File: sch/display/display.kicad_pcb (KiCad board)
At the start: 2 copper layers, 76.2 x 45.7 mm, 17 parts, among them IC1 MAX7219, P1 INPUT, P2 CONN_1, P3 CONN_1, P4 CONN_1, P5 CONN_1, P6 OUTPUT

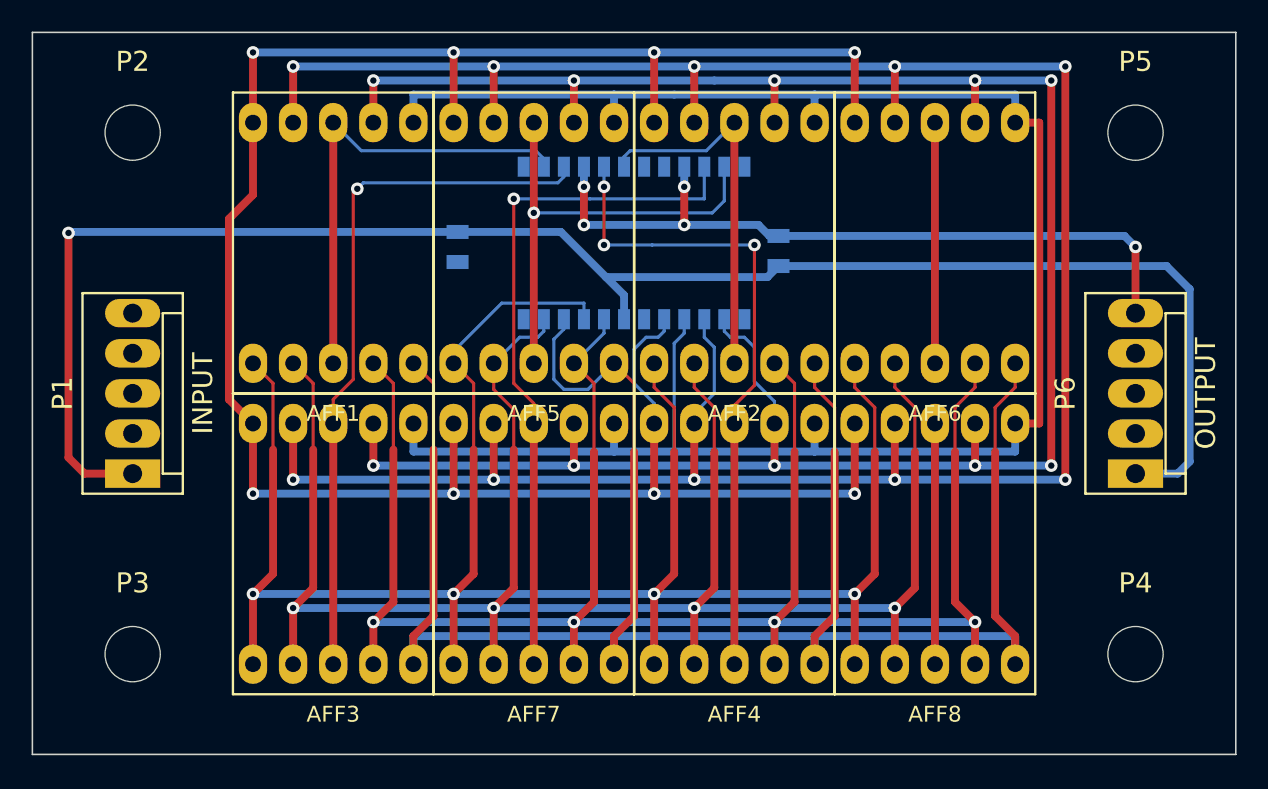
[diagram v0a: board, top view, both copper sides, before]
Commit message: Finished layout of the display.  Not really happy with it though.
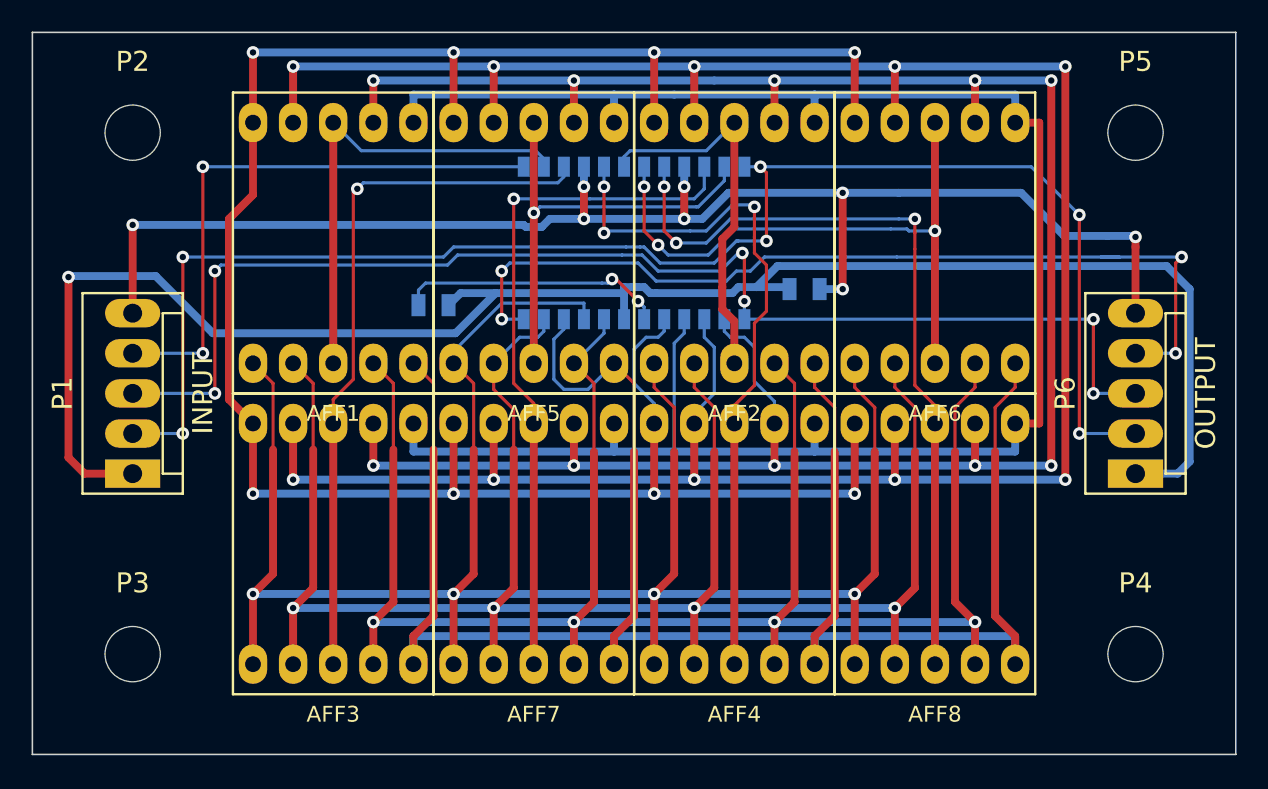
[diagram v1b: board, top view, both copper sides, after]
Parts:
- moved R1 3.99 mm to (123.2, 100.5), turned to 180 degrees
- moved C1 2.92 mm to (146.7, 99.4), turned to 0 degrees
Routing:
- net /LOAD: track 0.00 -> 97.3 mm, vias 0 -> 6
- net /SCK: track 0.00 -> 81.4 mm, vias 0 -> 6
- net /DO: track 0.00 -> 58.8 mm, vias 0 -> 4
- net GND: track 47.1 -> 90.2 mm, vias 5 -> 8
- net /DI: track 0.00 -> 36.6 mm, vias 0 -> 2
- net /DIG7: track 15.2 -> 49.6 mm, vias 0 -> 3
- net /DIG3: track 15.2 -> 39.1 mm, vias 0 -> 3
- net Net-(IC1-Pad18): track 0.00 -> 17.0 mm, vias 0 -> 2
- net +5V: track 109.6 -> 113.2 mm
- net /DIG6: track 41.5 -> 44.6 mm
- net /DIG1: track 29.8 -> 29.0 mm
- net /DIG2: track 23.8 -> 24.4 mm

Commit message: Fiddling with the layout of the display to make it more elegant.
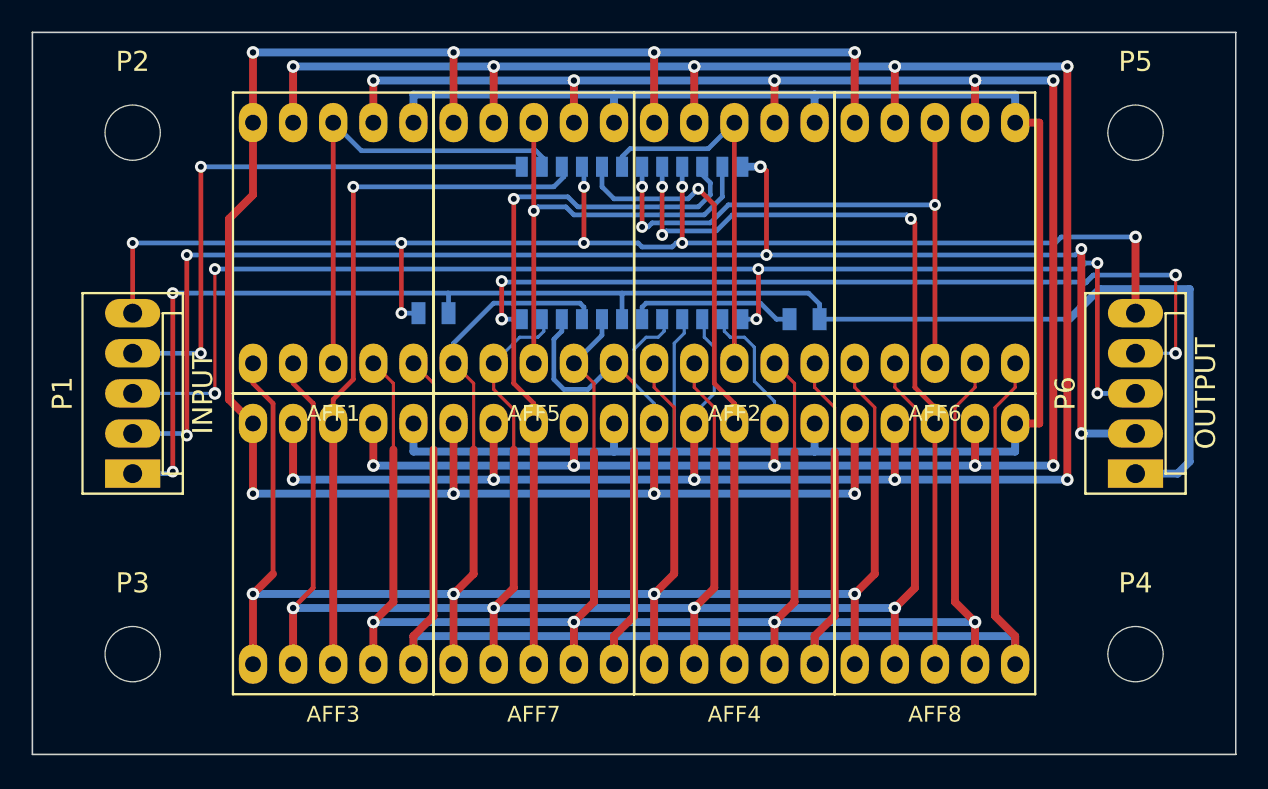
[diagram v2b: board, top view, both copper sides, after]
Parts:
- moved C1 23.5 mm to (123.2, 101.0), turned to 180 degrees
- moved R1 23.5 mm to (146.7, 101.3)
- moved IC1 0.13 mm to (135.8, 96.5)
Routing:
- net +5V: track 113.2 -> 98.0 mm, vias 1 -> 2
- net Net-(IC1-Pad18): track 17.0 -> 10.6 mm, vias 2 -> 0
- net /DIG6: track 44.6 -> 40.3 mm, vias 3 -> 1
- net /DO: track 58.8 -> 55.1 mm
- net /LOAD: track 97.3 -> 93.7 mm
- net /SCK: track 81.4 -> 83.9 mm
- net GND: track 90.2 -> 88.3 mm
- net /DIG5: track 43.7 -> 45.1 mm
- net /DIG7: track 49.6 -> 50.7 mm
- net /DIG3: track 39.1 -> 38.2 mm
- net /SEGE: track 129.8 -> 130.7 mm
- net /DIG1: track 29.0 -> 29.9 mm
- net /SEGF: track 160.7 -> 160.0 mm
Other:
- net class Default: trace_width 0.5 -> 0.3; via_dia 0.8 -> 0.75; via_drill 0.5 -> 0.4

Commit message: Happy with the display module now.  Not done gerbers/drill yet but layout is done incl. silk screen.
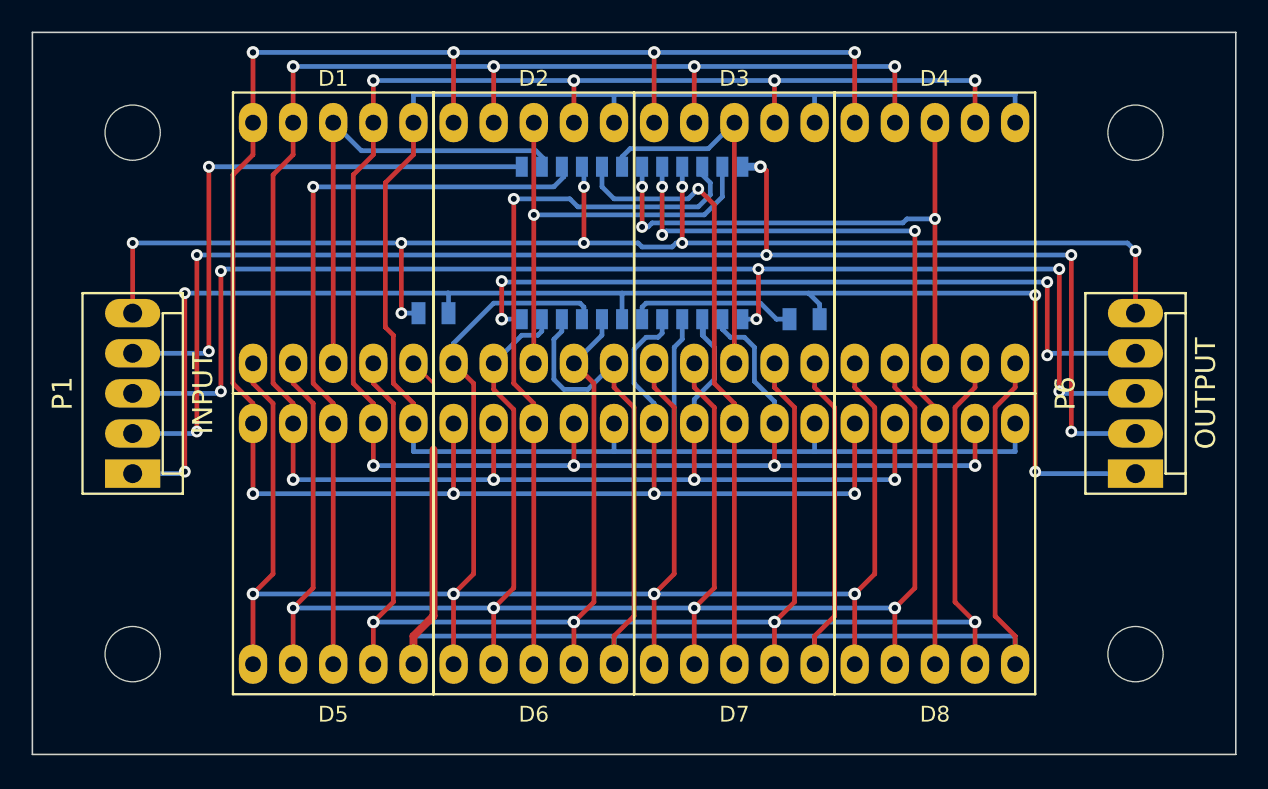
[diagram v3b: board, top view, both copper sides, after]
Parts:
- removed AFF1, AFF2, AFF3, AFF4, AFF5, AFF6, AFF7, AFF8: 7SEGMENTS, Nathan_THT:7SEGM_LED_0_5_INCH
- added D1: 7SEGMENTS, Nathan_THT:7SEGM_LED_0_5_INCH, F.Cu at (116.8, 96.5)
- added D2: 7SEGMENTS, Nathan_THT:7SEGM_LED_0_5_INCH, F.Cu at (129.5, 96.5)
- added D3: 7SEGMENTS, Nathan_THT:7SEGM_LED_0_5_INCH, F.Cu at (142.2, 96.5)
- added D4: 7SEGMENTS, Nathan_THT:7SEGM_LED_0_5_INCH, F.Cu at (154.9, 96.5)
- added D5: 7SEGMENTS, Nathan_THT:7SEGM_LED_0_5_INCH, F.Cu at (116.8, 115.6)
- added D6: 7SEGMENTS, Nathan_THT:7SEGM_LED_0_5_INCH, F.Cu at (129.5, 115.6)
- added D7: 7SEGMENTS, Nathan_THT:7SEGM_LED_0_5_INCH, F.Cu at (142.2, 115.6)
- added D8: 7SEGMENTS, Nathan_THT:7SEGM_LED_0_5_INCH, F.Cu at (154.9, 115.6)
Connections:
- P2 pad 1: Net-(P2-Pad1) -> (no net)
- P3 pad 1: Net-(P3-Pad1) -> (no net)
- P4 pad 1: Net-(P4-Pad1) -> (no net)
- P5 pad 1: Net-(P5-Pad1) -> (no net)
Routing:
- net /SEGF: track 160.0 -> 134.2 mm, vias 10 -> 8
- net /SEGA: track 140.3 -> 127.4 mm, vias 10 -> 8
- net +5V: track 98.0 -> 91.1 mm, vias 2 -> 4
- net /DO: track 55.1 -> 48.7 mm
- net /DIG4: track 45.0 -> 47.5 mm
- net /SEGB: track 121.2 -> 119.5 mm
- net /SEGG: track 141.3 -> 140.2 mm
- net /DIG7: track 50.7 -> 49.5 mm
- net /LOAD: track 93.7 -> 92.8 mm
- net GND: track 88.3 -> 87.5 mm
- net /SCK: track 83.9 -> 83.1 mm

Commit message: Final changes before ordering PCBs
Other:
- board text added: "7 Segment Display Module Copyright Nathan Dumont 2014 CC-BY"
- board text added: "REV A - 2014-05-18"
